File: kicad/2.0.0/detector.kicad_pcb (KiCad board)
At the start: 2 copper layers, 58 parts, among them U1 LT1761-5, U2 LT1964-5, U3 REF5010ID, U4 OPA2197xD, U5 OPA2197xD

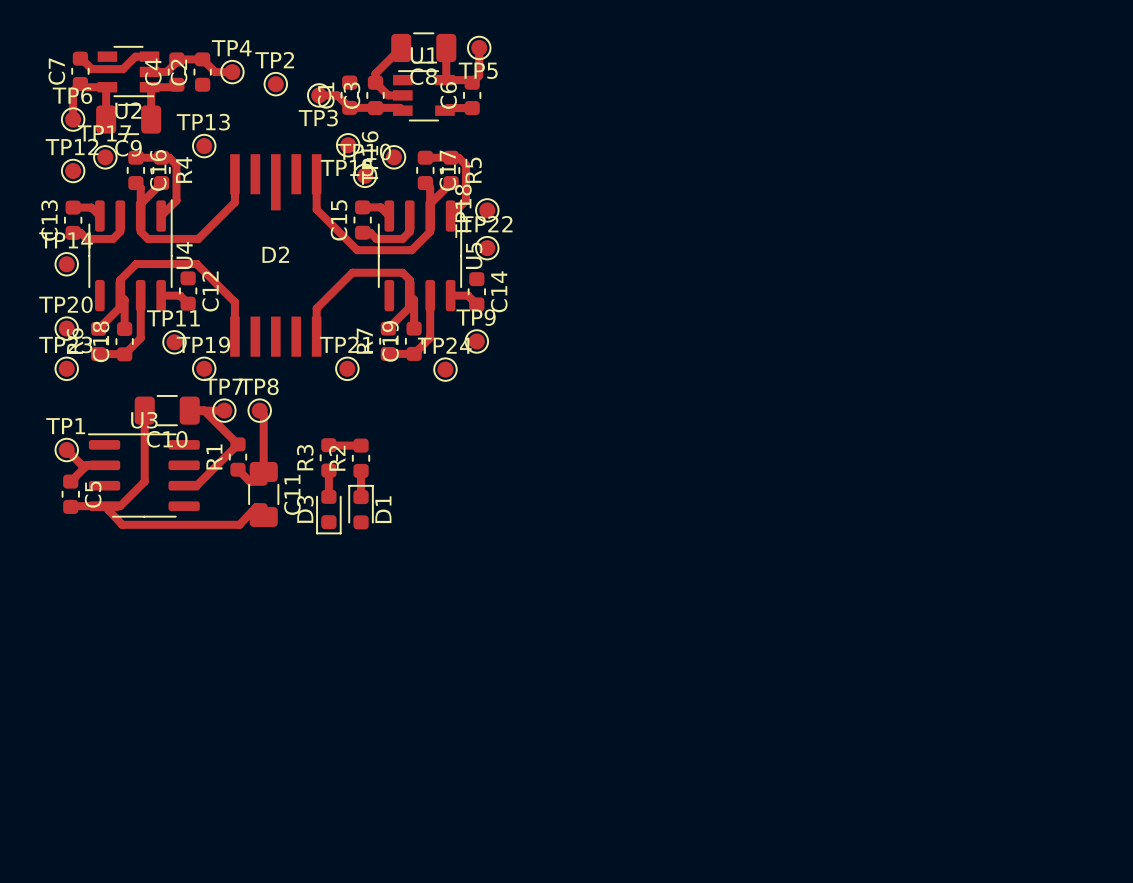
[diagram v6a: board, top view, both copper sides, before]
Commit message: created common symbol and footprint library, completed placement of components of 2.0.0 detector
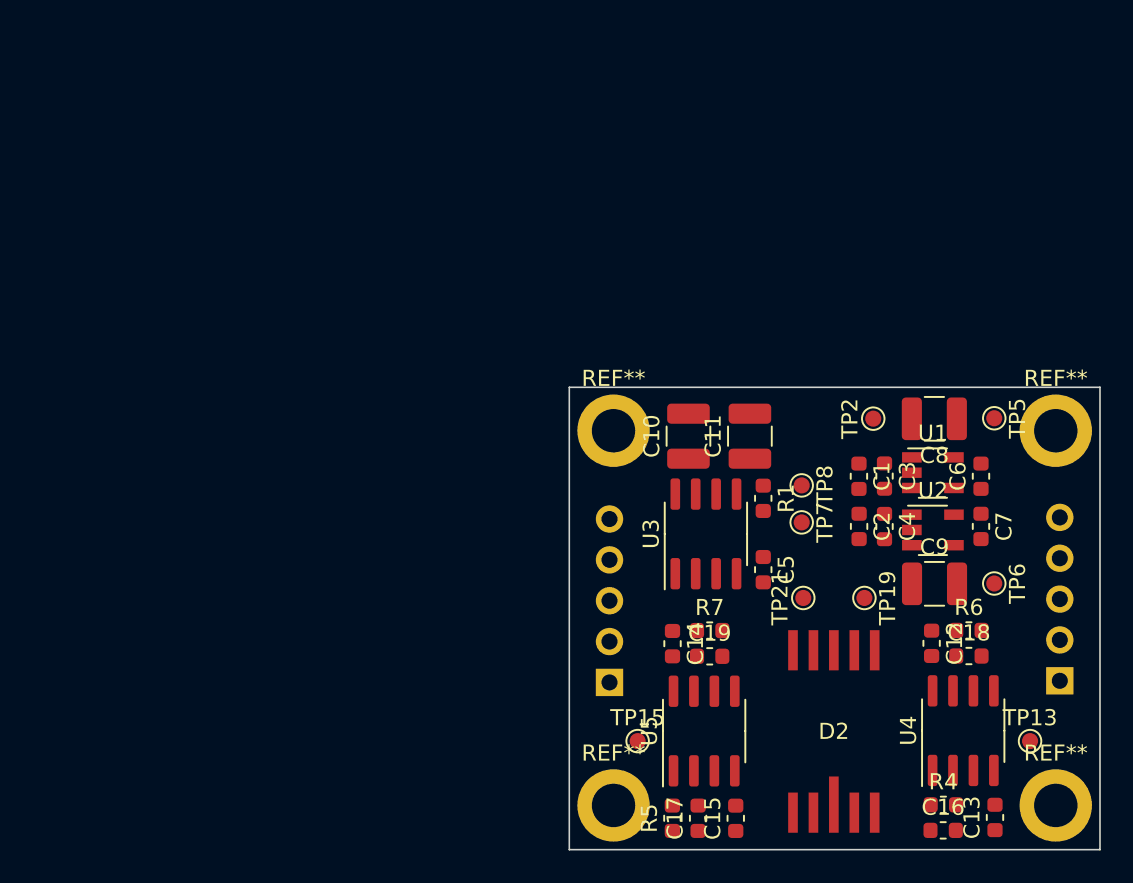
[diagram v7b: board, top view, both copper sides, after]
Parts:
- removed D1, D3: LED, Diode_SMD:D_0603_1608Metric
- removed R2: 130, Resistor_SMD:R_0603_1608Metric
- removed R3: 160, Resistor_SMD:R_0603_1608Metric
- removed TP1, TP3: +15V, TestPoint:TestPoint_Pad_D1.0mm
- removed TP10, TP12: -5V, TestPoint:TestPoint_Pad_D1.0mm
- removed TP11, TP9: +5V, TestPoint:TestPoint_Pad_D1.0mm
- removed TP14: -X1+, TestPoint:TestPoint_Pad_D1.0mm
- removed TP16: -Y1+, TestPoint:TestPoint_Pad_D1.0mm
- removed TP17: -X1, TestPoint:TestPoint_Pad_D1.0mm
- removed TP18: -Y1, TestPoint:TestPoint_Pad_D1.0mm
- removed TP20: -Y2+, TestPoint:TestPoint_Pad_D1.0mm
- removed TP22: -X2+, TestPoint:TestPoint_Pad_D1.0mm
- removed TP23: -Y2, TestPoint:TestPoint_Pad_D1.0mm
- removed TP24: -X2, TestPoint:TestPoint_Pad_D1.0mm
- removed TP4: -15V, TestPoint:TestPoint_Pad_D1.0mm
- added J1: Conn_01x05_Male, Connector_PinSocket_2.54mm:PinSocket_1x05_P2.54mm_Vertical, B.Cu at (95.2, 139.8)
- added J2: Conn_01x05_Male, Connector_PinSocket_2.54mm:PinSocket_1x05_P2.54mm_Vertical, B.Cu at (123.2, 139.8)
- added REF**: MountingHole_2.7mm_M2.5_ISO7380_Pad, MountingHole:MountingHole_2.7mm_M2.5_ISO7380_Pad, F.Cu at (95.5, 124.2)
- added REF**: MountingHole_2.7mm_M2.5_ISO7380_Pad, MountingHole:MountingHole_2.7mm_M2.5_ISO7380_Pad, F.Cu at (123.0, 124.2)
- added REF**: MountingHole_2.7mm_M2.5_ISO7380_Pad, MountingHole:MountingHole_2.7mm_M2.5_ISO7380_Pad, F.Cu at (95.5, 147.5)
- added REF**: MountingHole_2.7mm_M2.5_ISO7380_Pad, MountingHole:MountingHole_2.7mm_M2.5_ISO7380_Pad, F.Cu at (123.0, 147.5)
- C10, C11, C8, C9: footprint Capacitor_SMD:C_1206_3216Metric -> Capacitor_SMD:C_1210_3225Metric
- D2: footprint Sensor_Optical_Position:S5990 -> Common:S5990
- TP13: value -X1- -> I1
- TP15: value -Y1- -> I3
- TP19: value -Y2- -> I4
- TP21: value -X2- -> I2
- moved C13 68.3 mm to (119.2, 148.2)
- moved C16 64.8 mm to (116.0, 149.1), turned to 0 degrees
- moved TP6 64.1 mm to (119.2, 133.7), turned to 270 degrees
- moved TP13 63.3 mm to (121.4, 143.5)
- moved C7 62.7 mm to (118.3, 130.2), turned to 270 degrees
- moved R4 62.6 mm to (116.0, 147.5), turned to 0 degrees
- moved U4 59.6 mm to (117.2, 142.8), turned to 90 degrees
- moved C9 57.8 mm to (115.5, 133.7), turned to 0 degrees
- moved U2 57.6 mm to (115.4, 130.4), turned to 0 degrees
- moved R6 57.0 mm to (117.6, 136.6), turned to 0 degrees
- moved C18 56.0 mm to (117.6, 138.2), turned to 0 degrees
- moved C4 52.3 mm to (112.3, 130.2), turned to 270 degrees
- moved C12 51.2 mm to (115.3, 137.4)
- moved C2 49.6 mm to (110.8, 130.2), turned to 270 degrees
- moved D2 45.6 mm to (109.2, 142.9), turned to 180 degrees
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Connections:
- net +15V renamed +12V
- net -15V renamed -12V
- C1 pad 2: Net-(C1-Pad2) -> GND
- C2 pad 1: Net-(C1-Pad2) -> GND
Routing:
- net GND: track 39.7 -> 0.00 mm
- net Net-(C17-Pad2): track 16.5 -> 0.00 mm
- net Net-(C18-Pad2): track 16.4 -> 0.00 mm
- net Net-(C16-Pad2): track 14.5 -> 0.00 mm
- net Net-(C19-Pad2): track 14.4 -> 0.00 mm
- net +12V: track 10.9 -> 0.00 mm
- net Net-(C10-Pad1): track 10.4 -> 0.00 mm
- net -5V: track 10.2 -> 0.00 mm
- net +5V: track 9.88 -> 0.00 mm
- net /-Y1: track 6.28 -> 0.00 mm
- net /-X1: track 6.28 -> 0.00 mm
- net Net-(C11-Pad1): track 5.83 -> 0.00 mm
- net -12V: track 5.80 -> 0.00 mm
- net /-Y2: track 5.68 -> 0.00 mm
- net /-X2: track 5.64 -> 0.00 mm
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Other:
- board outline added: 33 x 28.8 mm

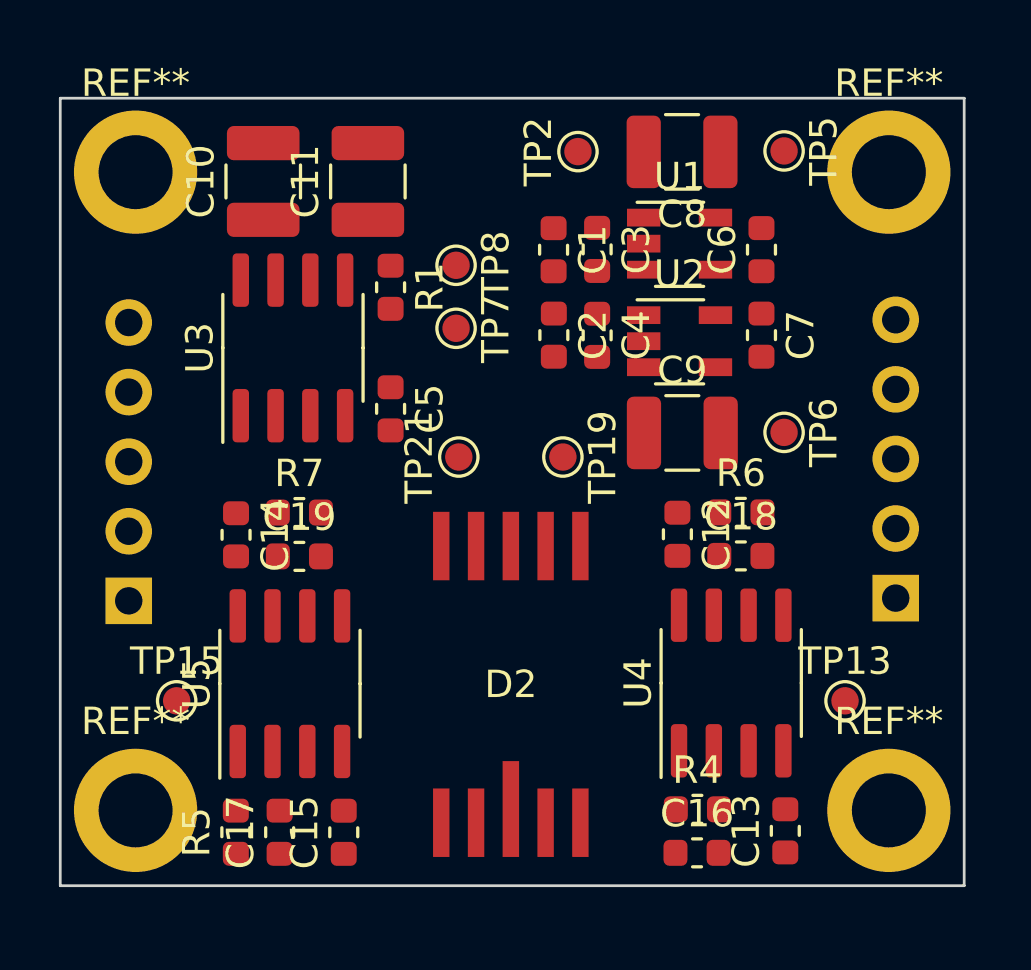
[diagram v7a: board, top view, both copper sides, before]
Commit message: routed traces for 2.0.0 pcbs
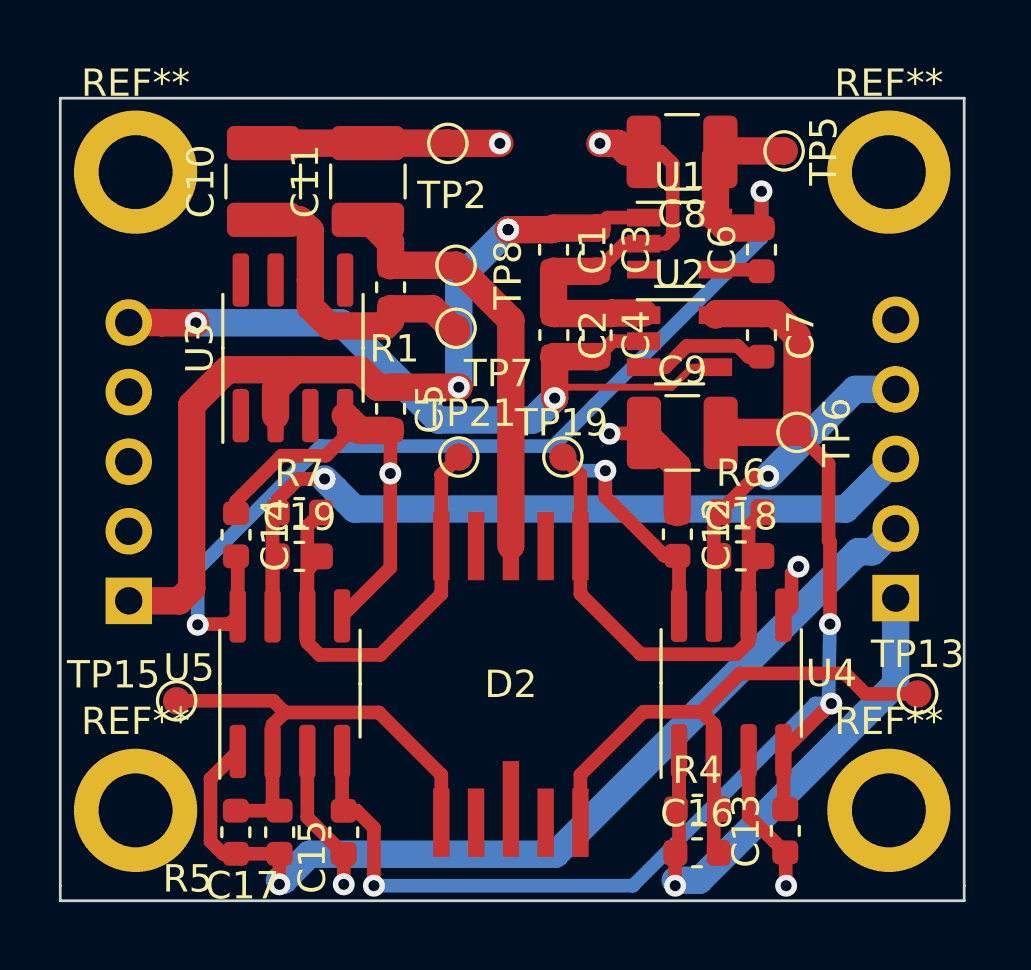
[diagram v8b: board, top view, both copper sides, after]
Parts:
- moved TP2 4.76 mm to (106.9, 123.2)
- moved TP13 2.66 mm to (124.0, 143.2)
- moved TP6 0.48 mm to (119.7, 133.7)
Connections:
- J2 pad 2: /-X2 -> /-Y1
- J2 pad 3: /-Y1 -> /-X2
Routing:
- net GND: track 0.00 -> 57.6 mm, vias 0 -> 7
- net -5V: track 0.00 -> 50.0 mm, vias 0 -> 3
- net +5V: track 0.00 -> 50.0 mm, vias 0 -> 3
- net /-Y1: track 0.00 -> 35.4 mm, vias 0 -> 1
- net +12V: track 0.00 -> 33.3 mm, vias 0 -> 3
- net /-X2: track 0.00 -> 30.7 mm, vias 0 -> 1
- net -12V: track 0.00 -> 28.7 mm, vias 0 -> 2
- net Net-(C16-Pad2): track 0.00 -> 23.5 mm
- net /-X1: track 0.00 -> 21.3 mm, vias 0 -> 1
- net Net-(C18-Pad2): track 0.00 -> 19.8 mm
- net Net-(C19-Pad2): track 0.00 -> 18.6 mm
- net Net-(C17-Pad2): track 0.00 -> 18.0 mm
- net Net-(C11-Pad1): track 0.00 -> 15.5 mm
- net /-Y2: track 0.00 -> 14.4 mm, vias 0 -> 1
- net Net-(C10-Pad1): track 0.00 -> 11.3 mm
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- added copper zone on In1.Cu, net GND
- added copper zone on In2.Cu, net GND
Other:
- board size 33 x 28.8 mm -> 33 x 29.3 mm
- copper layers 2 -> 4
